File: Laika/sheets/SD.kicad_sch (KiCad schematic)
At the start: 0 parts

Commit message: Added SD card power source selector and boot medium selector.
The SD card power source (VDD_SD) can be selected between a software
managed 3.3V power supply (PWR_SD_SW); or through the 3.3V power rail
(+3V3). Doubles as selector whether to boot from SD card or eMMC.
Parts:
- added C10: 10u, symbol Device:C
- added J4: Conn_01x03, symbol Connector_Generic:Conn_01x03
- added Q3: Q_NPN, symbol Device:Q_NPN
- added Q4: Q_PMOS, symbol Device:Q_PMOS
- added R17, R19: 10k, symbol Device:R
- added R20: 100k, symbol Device:R
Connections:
- new net: Q3.B, R17.2
- new net: Q3.C, R19.1
- new net +3V3: J4.1 (Pin_1), Q4.S, R20.1
- new net GND: C10.2, Q3.E
- new net PWR_SD_SW: C10.1, J4.3 (Pin_3), Q4.D
- new net SD_PWR_EN: R17.1
- new net SD_PWR_FET_GATE: Q4.G, R19.2, R20.2
- new net VDD_SD: J4.2 (Pin_2)
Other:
- note added: "PWR_SD_SW is a software controlled power rail for the SD Card"
- note added: "R19: Strong pulldown to GND R20: Weak pullup to 3V3."
- note added: "SD Card Power Enable/Disable"
- note added: "SD Card Power Select/Boot medium select"
- note added: "To boot from SD card, add a jumper between SD power (VDD_SD) and +3V3. To use SD card for user purposes, (boot from eMMC) connect it to PWR_SD_SW"

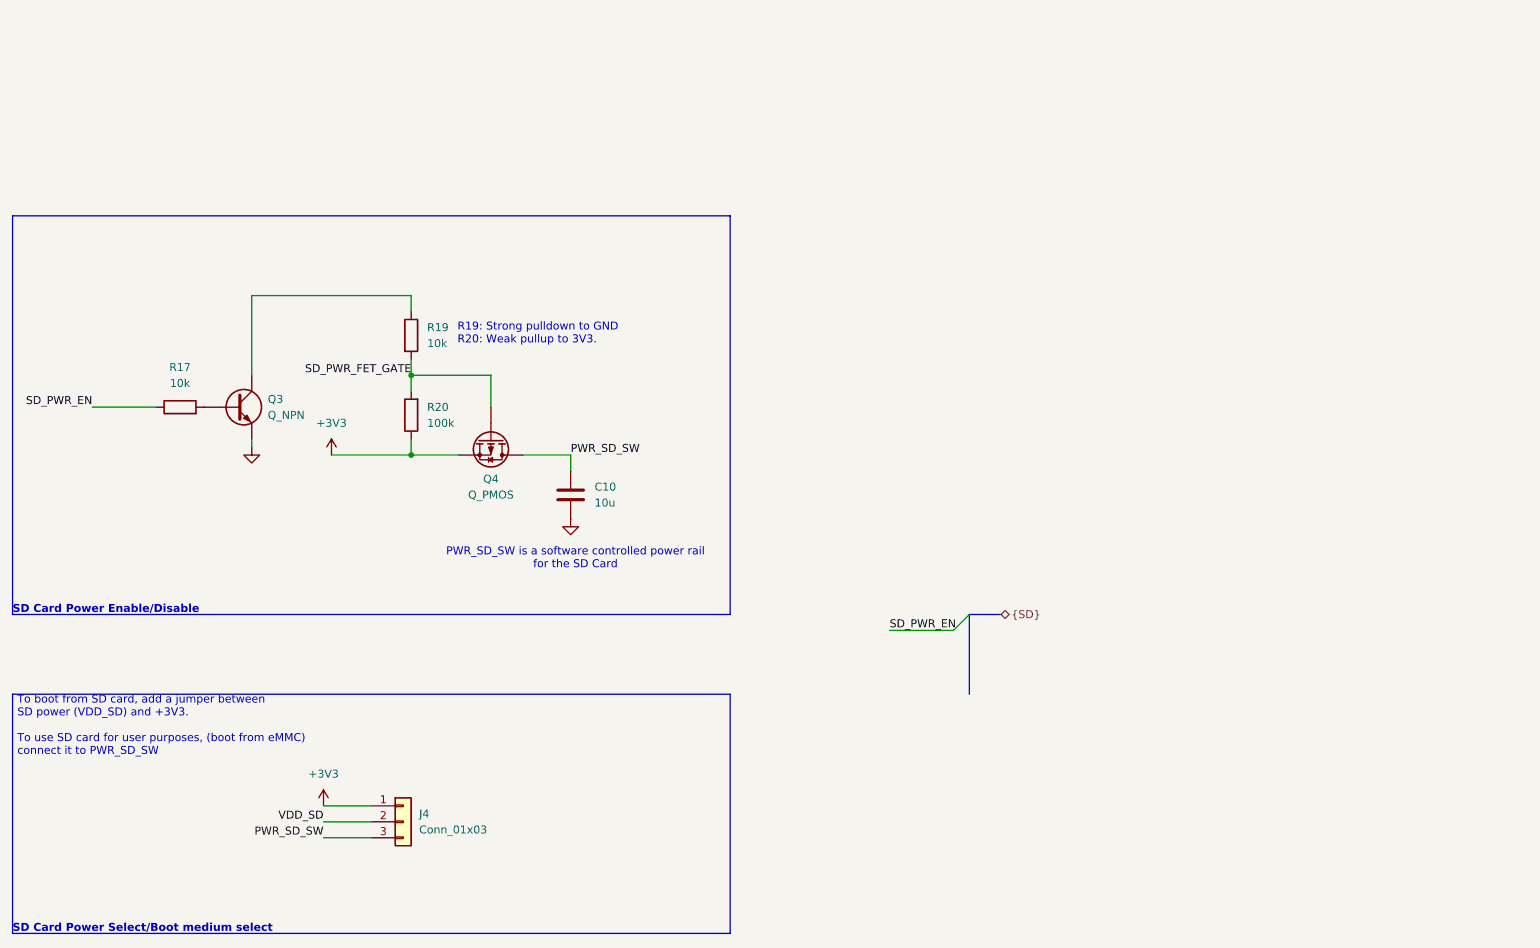
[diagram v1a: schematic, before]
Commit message: Completed microSD card receptacle block
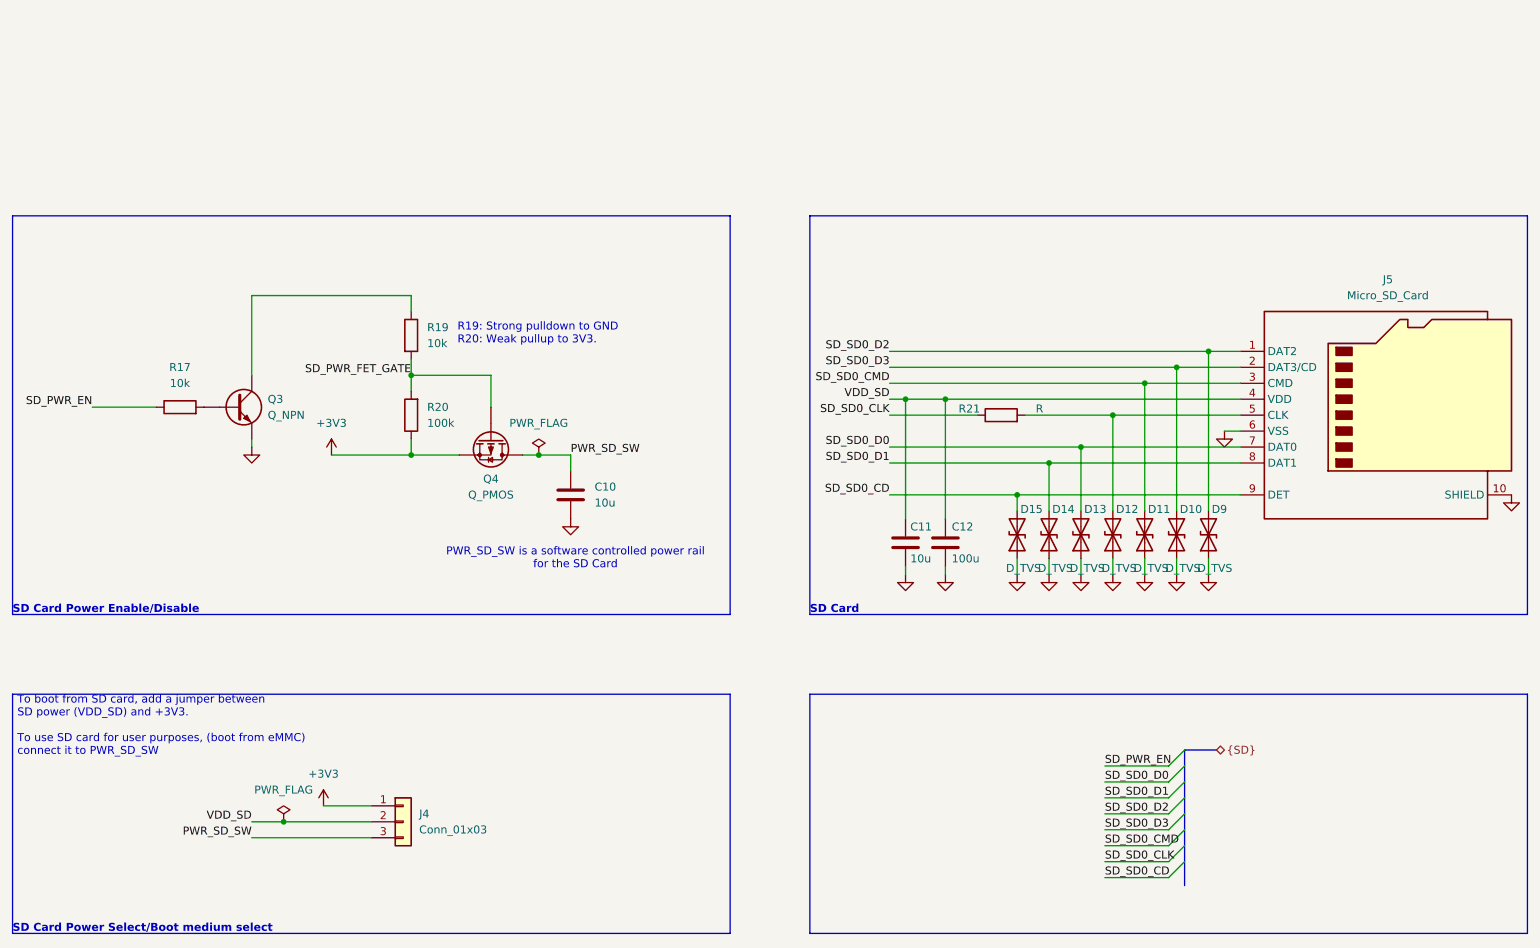
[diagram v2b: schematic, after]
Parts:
- added C11: 10u, symbol Device:C
- added C12: 100u, symbol Device:C
- added D10, D11, D12, D13, D14, D15, D9: D_TVS, symbol Device:D_TVS
- added J5: Micro_SD_Card, symbol Connector:Micro_SD_Card_Det1
- added R21: R, symbol Device:R
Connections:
- net GND: now also C11.2, C12.2, D10.1 (A1), D11.1 (A1), D12.1 (A1), D13.1 (A1), D14.1 (A1), D15.1 (A1), D9.1 (A1), J5.10 (SHIELD), J5.6 (VSS)
- net VDD_SD: now also C11.1, C12.1, J5.4 (VDD)
- new net: D12.2 (A2), J5.5 (CLK), R21.2
- new net SD_SD0_CD: D15.2 (A2), J5.9 (DET)
- new net SD_SD0_CLK: R21.1
- new net SD_SD0_CMD: D11.2 (A2), J5.3 (CMD)
- new net SD_SD0_D0: D13.2 (A2), J5.7 (DAT0)
- new net SD_SD0_D1: D14.2 (A2), J5.8 (DAT1)
- new net SD_SD0_D2: D9.2 (A2), J5.1 (DAT2)
- new net SD_SD0_D3: D10.2 (A2), J5.2 (DAT3/CD)
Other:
- note added: "SD Card"

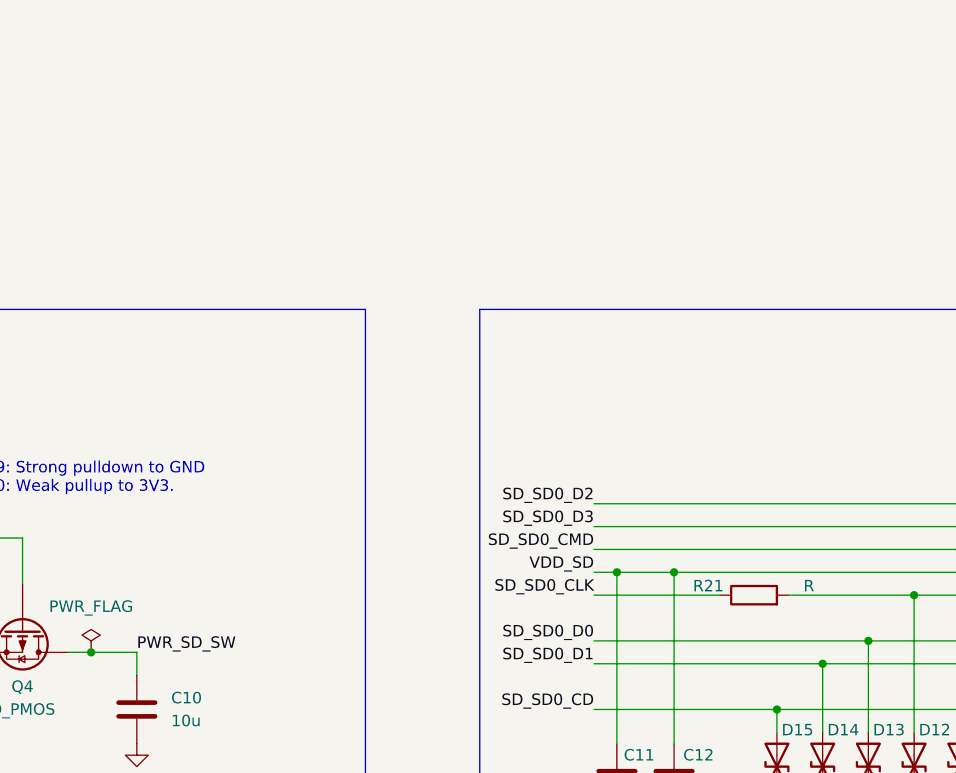
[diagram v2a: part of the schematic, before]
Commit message: Added headers for system uart console. DNP for SD CLK.
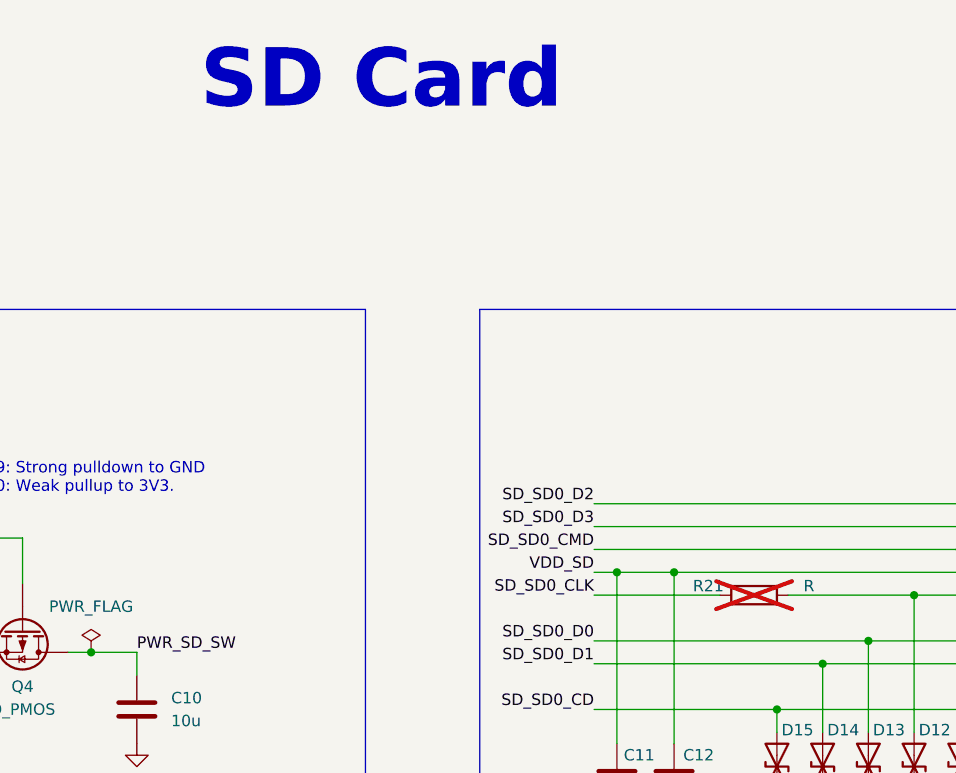
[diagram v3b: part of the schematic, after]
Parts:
- R21: now not fitted
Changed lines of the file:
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@@
+		)
+	)
+	(text "SD Card"
+		(exclude_from_sim no)
+		(at 141.478 25.4 0)
+		(effects
+			(font
+				(size 6.5024 6.5024)
+				(thickness 0.254)
+				(bold yes)
+			)
 		)
 	)
@@
 		(in_bom yes)
 		(on_board yes)
-		(dnp no)
+		(dnp yes)
 		(property "Reference" "R21"
 			(at 177.8 81.534 90)

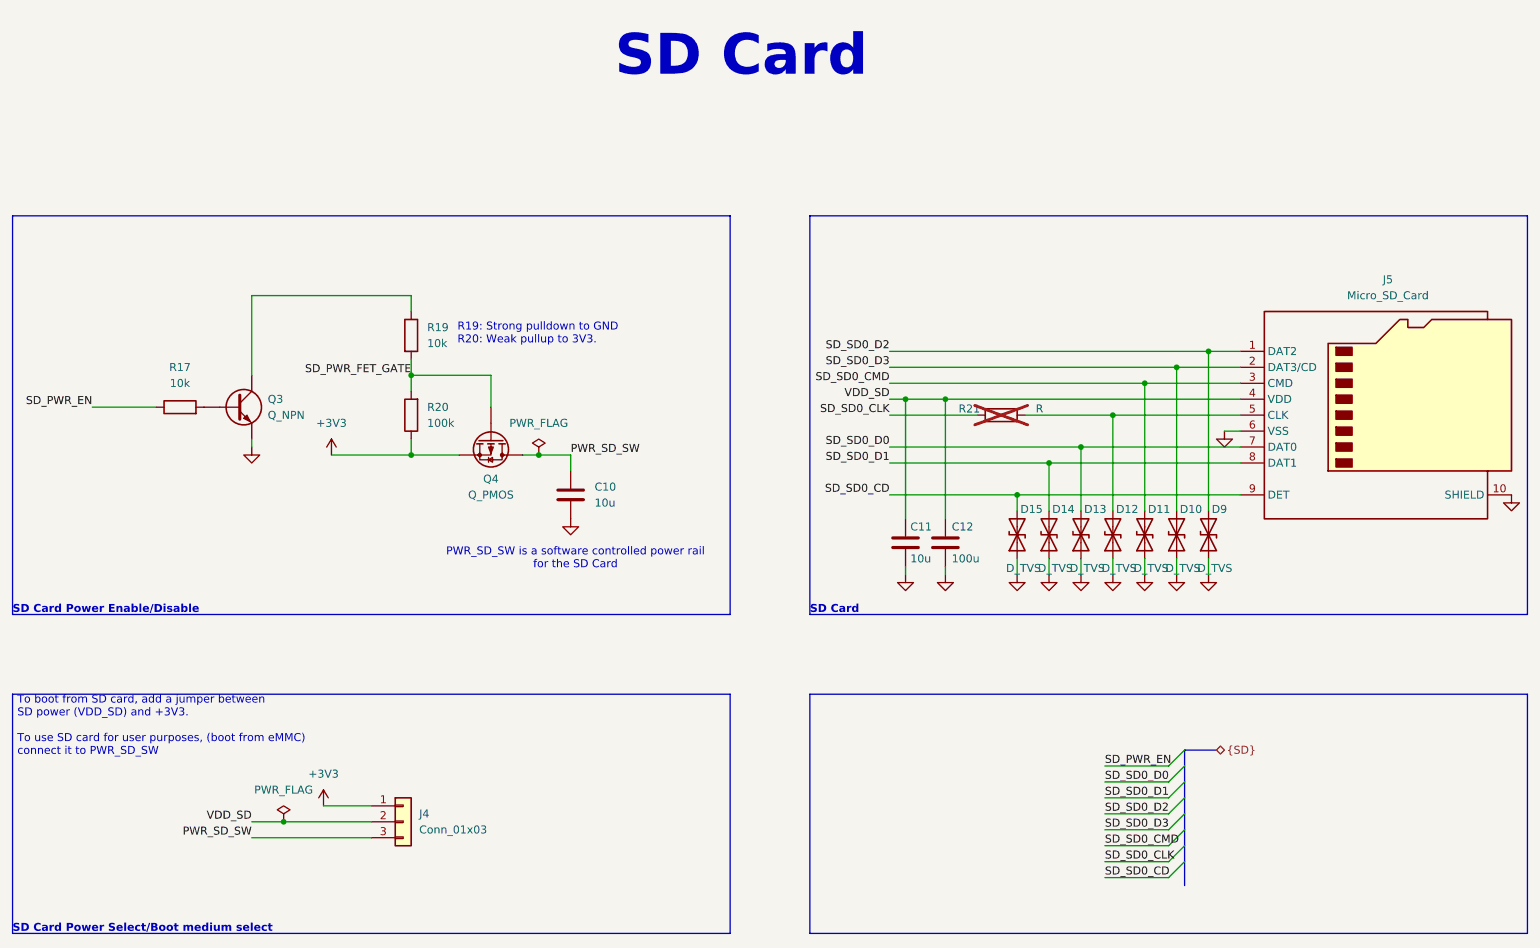
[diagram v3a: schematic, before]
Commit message: Populated BOM with part numbers and footprints
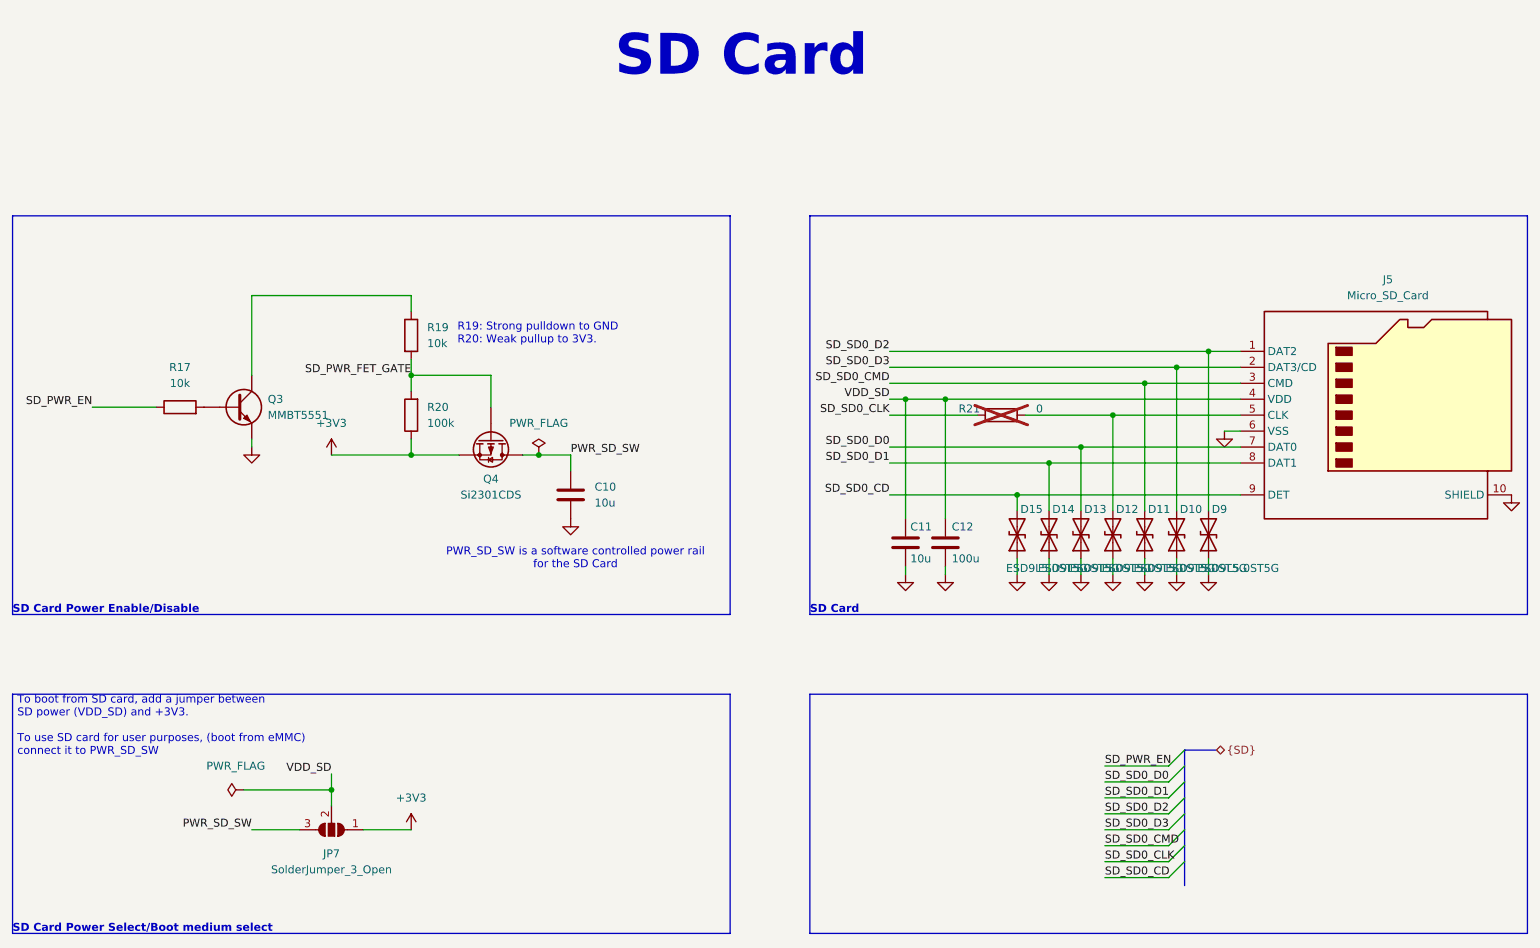
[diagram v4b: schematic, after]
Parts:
- removed J4: Conn_01x03, symbol Connector_Generic:Conn_01x03
- added JP7: SolderJumper_3_Open, Jumper:SolderJumper-3_P1.3mm_Open_Pad1.0x1.5mm, symbol Jumper:SolderJumper_3_Open
- C10, C11: footprint (none) -> Capacitor_SMD:C_0402_1005Metric; JLC Part Type (none) -> Basic; Manafacturer (none) -> Samsung Electro-Mechanics; Part Number (none) -> CL05A106MQ5NUNC
- C12: footprint (none) -> Capacitor_SMD:C_1206_3216Metric; JLC Part Type (none) -> Basic; Manafacturer (none) -> Samsung Electro-Mechanics; Part Number (none) -> CL31A107MQHNNNE
- D10, D11, D12, D13, D14, D15, D9: value D_TVS -> ESD9L5.0ST5G; footprint (none) -> Diode_SMD:D_SOD-923; JLC Part Type (none) -> Extended; Manafacturer (none) -> onsemi; Part Number (none) -> ESD9L5.0ST5G
- J5: footprint (none) -> Connector_Card:microSD_HC_Hirose_DM3AT-SF-PEJM5; JLC Part Type (none) -> Extended; Manafacturer (none) -> Hirose; Part Number (none) -> DM3AT-SF-PEJM5(41)
- Q3: value Q_NPN -> MMBT5551; footprint (none) -> Package_TO_SOT_SMD:SOT-23; JLC Part Type (none) -> Basic; Manafacturer (none) -> Diotec Semiconductor; Part Number (none) -> MMBT5551
- Q4: value Q_PMOS -> Si2301CDS; footprint (none) -> Package_TO_SOT_SMD:SOT-23-3; JLC Part Type (none) -> Basic; Manafacturer (none) -> Vishay Semiconductors; Part Number (none) -> SI2301CDS-T1-GE3
- R17, R19: footprint (none) -> Resistor_SMD:R_0402_1005Metric_Pad0.72x0.64mm_HandSolder; JLC Part Type (none) -> Basic; Manafacturer (none) -> Royalohm; Part Number (none) -> 0402WGJ0103TCE
- R20: footprint (none) -> Resistor_SMD:R_0402_1005Metric_Pad0.72x0.64mm_HandSolder; JLC Part Type (none) -> Basic; Manafacturer (none) -> Royalohm; Part Number (none) -> 0402WGF1003TCE
- R21: value R -> 0; footprint (none) -> Resistor_SMD:R_0402_1005Metric_Pad0.72x0.64mm_HandSolder
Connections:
- net +3V3: now also JP7.1 (A)
- net PWR_SD_SW: now also JP7.3 (B)
- net VDD_SD: now also JP7.2 (C)

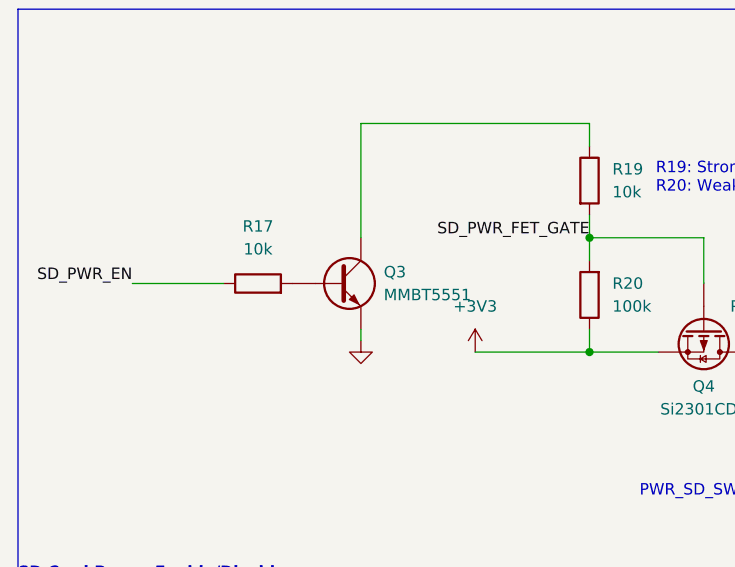
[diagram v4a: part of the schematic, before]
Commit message: Replace generic NPN with MMBT5551 symbol
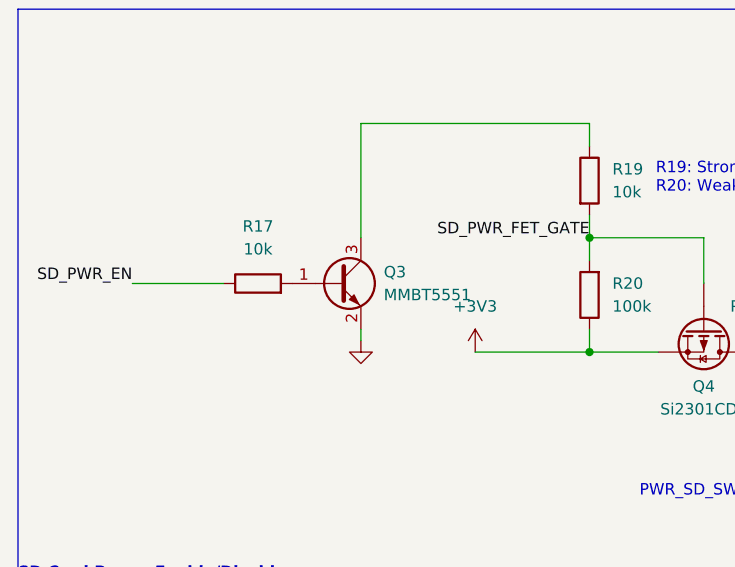
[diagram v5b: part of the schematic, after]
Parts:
- Q3: symbol Device:Q_NPN -> Transistor_BJT:MMBT5551L
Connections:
- net GND: now also Q3.2 (E); no longer Q3.E
- net at R17.2: now also Q3.1 (B); no longer Q3.B
- net at R19.1: now also Q3.3 (C); no longer Q3.C
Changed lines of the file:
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@@
 	)
 	(symbol
-		(lib_id "Device:Q_NPN")
+		(lib_id "Transistor_BJT:MMBT5551L")
 		(at 60.96 81.28 0)
 		(unit 1)
@@
 		)
 		(property "Footprint" "Package_TO_SOT_SMD:SOT-23"
-			(at 66.04 78.74 0)
+			(at 66.04 83.185 0)
 			(effects
 				(font
 					(size 1.27 1.27)
+					(italic yes)
 				)
+				(justify left)
 				(hide yes)
 			)
 		)
-		(property "Datasheet" "https://diotec.com/request/datasheet/mmbt5551.pdf"
+		(property "Datasheet" "www.onsemi.com/pub/Collateral/MMBT5550LT1-D.PDF"
 			(at 60.96 81.28 0)
 			(effects
@@
 					(size 1.27 1.27)
 				)
+				(justify left)
 				(hide yes)
 			)
 		)
-		(property "Description" "NPN bipolar junction transistor"
+		(property "Description" "0.6A Ic, 160V Vce, NPN Transistor, SOT-23"
 			(at 60.96 81.28 0)
 			(effects
@@
 			)
 		)
-		(pin "B"
+		(pin "1"
 		)
-		(pin "C"
+		(pin "2"
 		)
-		(pin "E"
+		(pin "3"
 		)
 		(instances
